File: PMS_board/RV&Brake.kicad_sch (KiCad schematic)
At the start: 24 parts, among them Q4 NMOS, Q5 NMOS, U19 TLV7011DCKR, U20 LT1910, U21 LM74700, U22 LM74700, U27 IRFS7530TRL7PP

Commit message: Add Footprints & such
whoops forgot to push yesterday teehee
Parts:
- C10, C11, C16, C9: footprint (none) -> Capacitor_SMD:C_0603_1608Metric
- U27: footprint PG-TO263-7_INF -> IRFS7530TRL7PP:PG-TO263-7_INF
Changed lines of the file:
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@@
 			)
 		)
-		(property "Footprint" "PG-TO263-7_INF"
+		(property "Footprint" "IRFS7530TRL7PP:PG-TO263-7_INF"
 			(at 104.14 160.02 0)
 			(hide yes)
@@
 			)
 		)
-		(property "Footprint" ""
+		(property "Footprint" "Capacitor_SMD:C_0603_1608Metric"
 			(at 255.27 113.03 0)
 			(hide yes)
@@
 			)
 		)
-		(property "Footprint" ""
+		(property "Footprint" "Capacitor_SMD:C_0603_1608Metric"
 			(at 187.6552 57.15 0)
 			(hide yes)
@@
 			)
 		)
-		(property "Footprint" ""
+		(property "Footprint" "Capacitor_SMD:C_0603_1608Metric"
 			(at 33.02 126.6952 0)
 			(hide yes)
@@
 			)
 		)
-		(property "Footprint" ""
+		(property "Footprint" "Capacitor_SMD:C_0603_1608Metric"
 			(at 187.6552 121.92 0)
 			(hide yes)

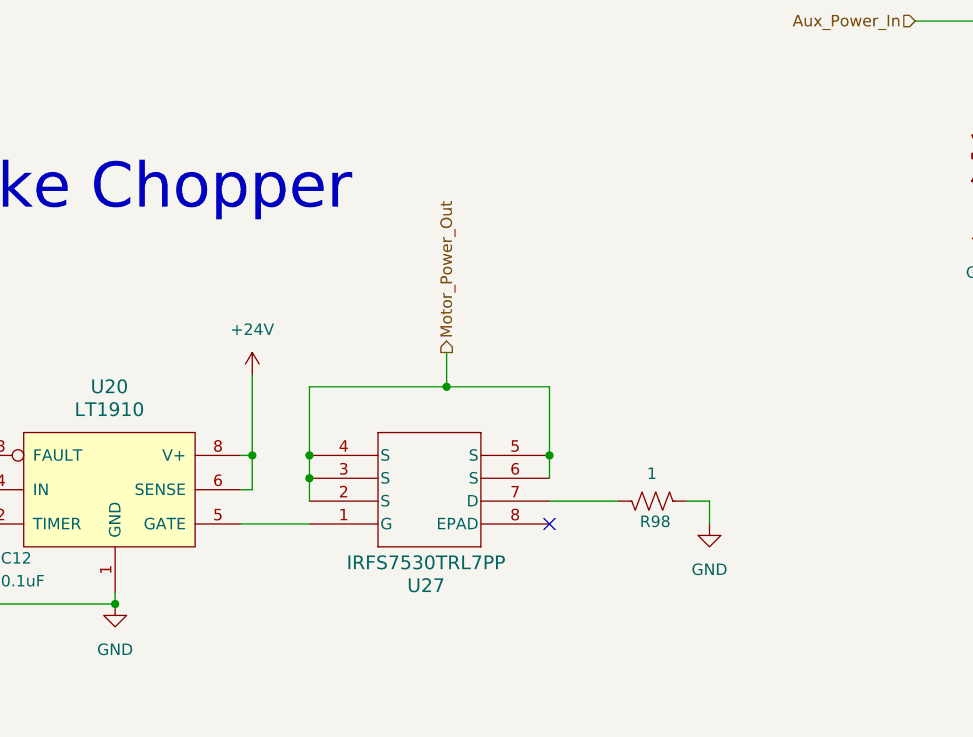
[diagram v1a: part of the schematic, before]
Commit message: Minor component tweaks and added a seperate LED sheet
Changed component values
Added labels
Moved LEDs to it's own sheet
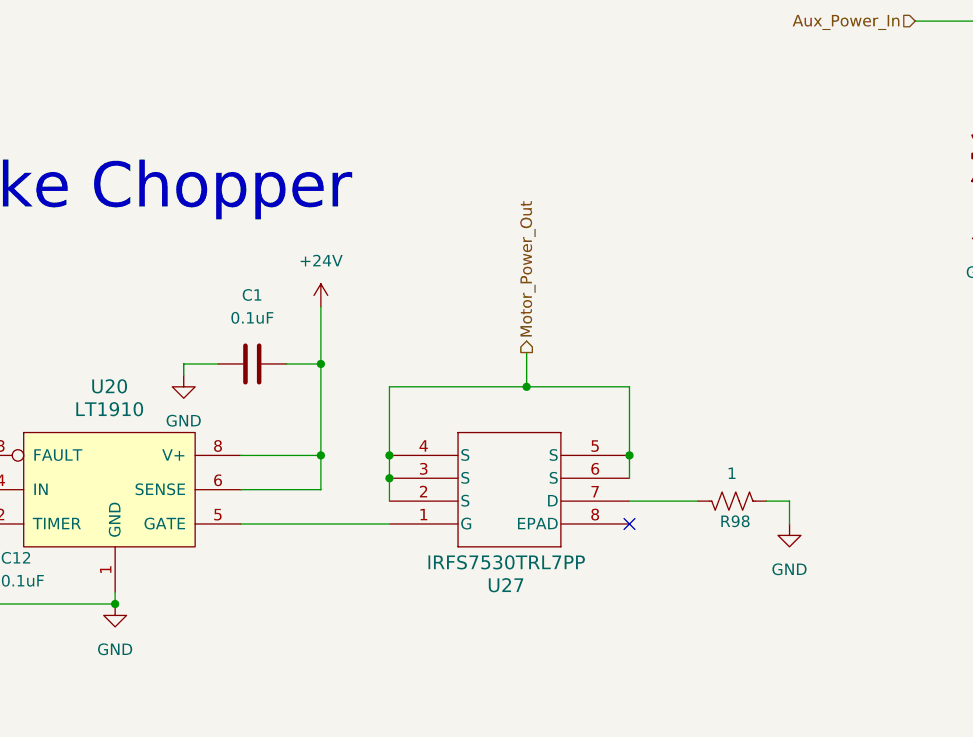
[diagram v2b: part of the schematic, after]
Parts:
- added C1: 0.1uF, symbol Device:C
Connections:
- net +24V: now also C1.2
- net GND: now also C1.1
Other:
- moved on the sheet: R98, U27

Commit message: How did our footprints get this geeked???
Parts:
- C1: footprint (none) -> Capacitor_SMD:C_0603_1608Metric_Pad1.08x0.95mm_HandSolder
- C12: footprint Package_SO:SOIC-8_3.9x4.9mm_P1.27mm -> Capacitor_SMD:C_0603_1608Metric_Pad1.08x0.95mm_HandSolder
- C13, C14, C15: footprint Package_SON:WSON-6-1EP_2x2mm_P0.65mm_EP1x1.6mm -> Capacitor_SMD:C_0603_1608Metric_Pad1.08x0.95mm_HandSolder
- C16: footprint Capacitor_SMD:C_0603_1608Metric -> Capacitor_SMD:C_0603_1608Metric_Pad1.08x0.95mm_HandSolder
- D24, D25: footprint Package_SON:WSON-8-1EP_6x5mm_P1.27mm_EP3.4x4mm -> (none)
- R92, R93, R94, R95, R96, R97: footprint (none) -> Resistor_SMD:R_0603_1608Metric_Pad0.98x0.95mm_HandSolder
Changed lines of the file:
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@@
 			)
 		)
-		(property "Footprint" "Package_SON:WSON-8-1EP_6x5mm_P1.27mm_EP3.4x4mm"
+		(property "Footprint" ""
 			(at 179.07 54.61 0)
 			(hide yes)
@@
 			)
 		)
-		(property "Footprint" ""
+		(property "Footprint" "Resistor_SMD:R_0603_1608Metric_Pad0.98x0.95mm_HandSolder"
 			(at 26.416 166.116 90)
 			(hide yes)
@@
 			)
 		)
-		(property "Footprint" "Capacitor_SMD:C_0603_1608Metric"
+		(property "Footprint" "Capacitor_SMD:C_0603_1608Metric_Pad1.08x0.95mm_HandSolder"
 			(at 255.27 113.03 0)
 			(hide yes)
@@
 			)
 		)
-		(property "Footprint" ""
+		(property "Footprint" "Capacitor_SMD:C_0603_1608Metric_Pad1.08x0.95mm_HandSolder"
 			(at 101.6 141.2748 0)
 			(hide yes)
@@
 			)
 		)
-		(property "Footprint" ""
+		(property "Footprint" "Resistor_SMD:R_0603_1608Metric_Pad0.98x0.95mm_HandSolder"
 			(at 26.416 152.146 90)
 			(hide yes)
@@
 			)
 		)
-		(property "Footprint" ""
+		(property "Footprint" "Resistor_SMD:R_0603_1608Metric_Pad0.98x0.95mm_HandSolder"
 			(at 29.464 159.766 90)
 			(hide yes)
@@
 			)
 		)
-		(property "Footprint" ""
+		(property "Footprint" "Resistor_SMD:R_0603_1608Metric_Pad0.98x0.95mm_HandSolder"
 			(at 38.354 143.256 90)
 			(hide yes)
@@
 			)
 		)
-		(property "Footprint" "Package_SON:WSON-6-1EP_2x2mm_P0.65mm_EP1x1.6mm"
+		(property "Footprint" "Capacitor_SMD:C_0603_1608Metric_Pad1.08x0.95mm_HandSolder"
 			(at 202.8952 123.19 0)
 			(hide yes)
@@
 			)
 		)
-		(property "Footprint" "Package_SON:WSON-6-1EP_2x2mm_P0.65mm_EP1x1.6mm"
+		(property "Footprint" "Capacitor_SMD:C_0603_1608Metric_Pad1.08x0.95mm_HandSolder"
 			(at 256.2352 55.88 0)
 			(hide yes)
@@
 			)
 		)
-		(property "Footprint" "Package_SON:WSON-8-1EP_6x5mm_P1.27mm_EP3.4x4mm"
+		(property "Footprint" ""
 			(at 179.07 119.38 0)
 			(hide yes)
@@
 			)
 		)
-		(property "Footprint" ""
+		(property "Footprint" "Resistor_SMD:R_0603_1608Metric_Pad0.98x0.95mm_HandSolder"
 			(at 45.974 169.926 90)
 			(hide yes)
@@
 			)
 		)
-		(property "Footprint" "Package_SO:SOIC-8_3.9x4.9mm_P1.27mm"
+		(property "Footprint" "Capacitor_SMD:C_0603_1608Metric_Pad1.08x0.95mm_HandSolder"
 			(at 67.0052 168.91 0)
 			(hide yes)
@@
 			)
 		)
-		(property "Footprint" "Package_SON:WSON-6-1EP_2x2mm_P0.65mm_EP1x1.6mm"
+		(property "Footprint" "Capacitor_SMD:C_0603_1608Metric_Pad1.08x0.95mm_HandSolder"
 			(at 202.8952 58.42 0)
 			(hide yes)
@@
 			)
 		)
-		(property "Footprint" ""
+		(property "Footprint" "Resistor_SMD:R_0603_1608Metric_Pad0.98x0.95mm_HandSolder"
 			(at 32.766 135.636 90)
 			(hide yes)
